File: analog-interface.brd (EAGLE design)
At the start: 160 x 100 mm, 18 parts, among them U1 ISL3179EIBZ, U2 ATMEGA328P

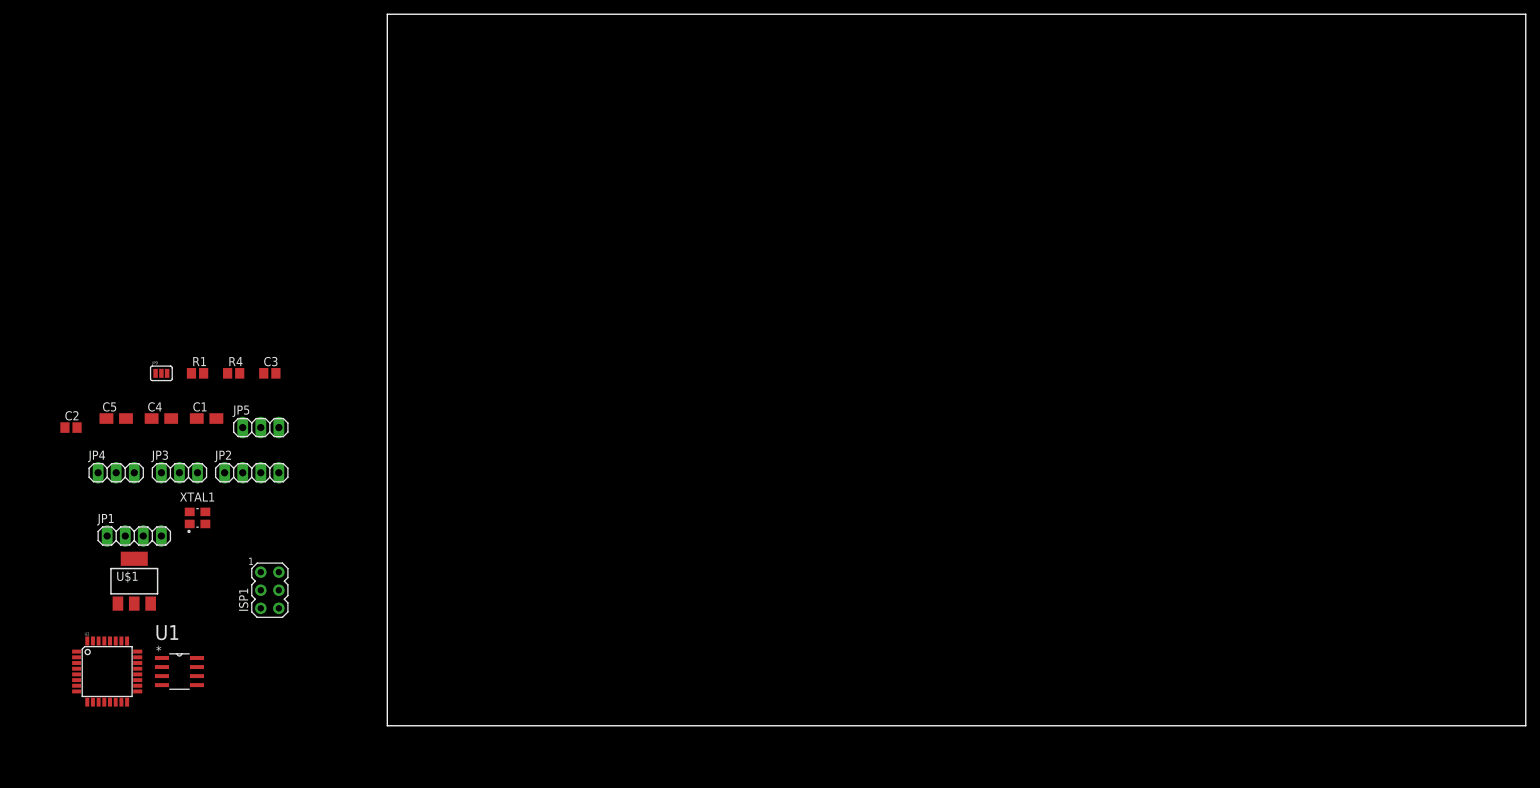
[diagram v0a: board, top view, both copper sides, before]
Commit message: done a lot of routing added vref chip
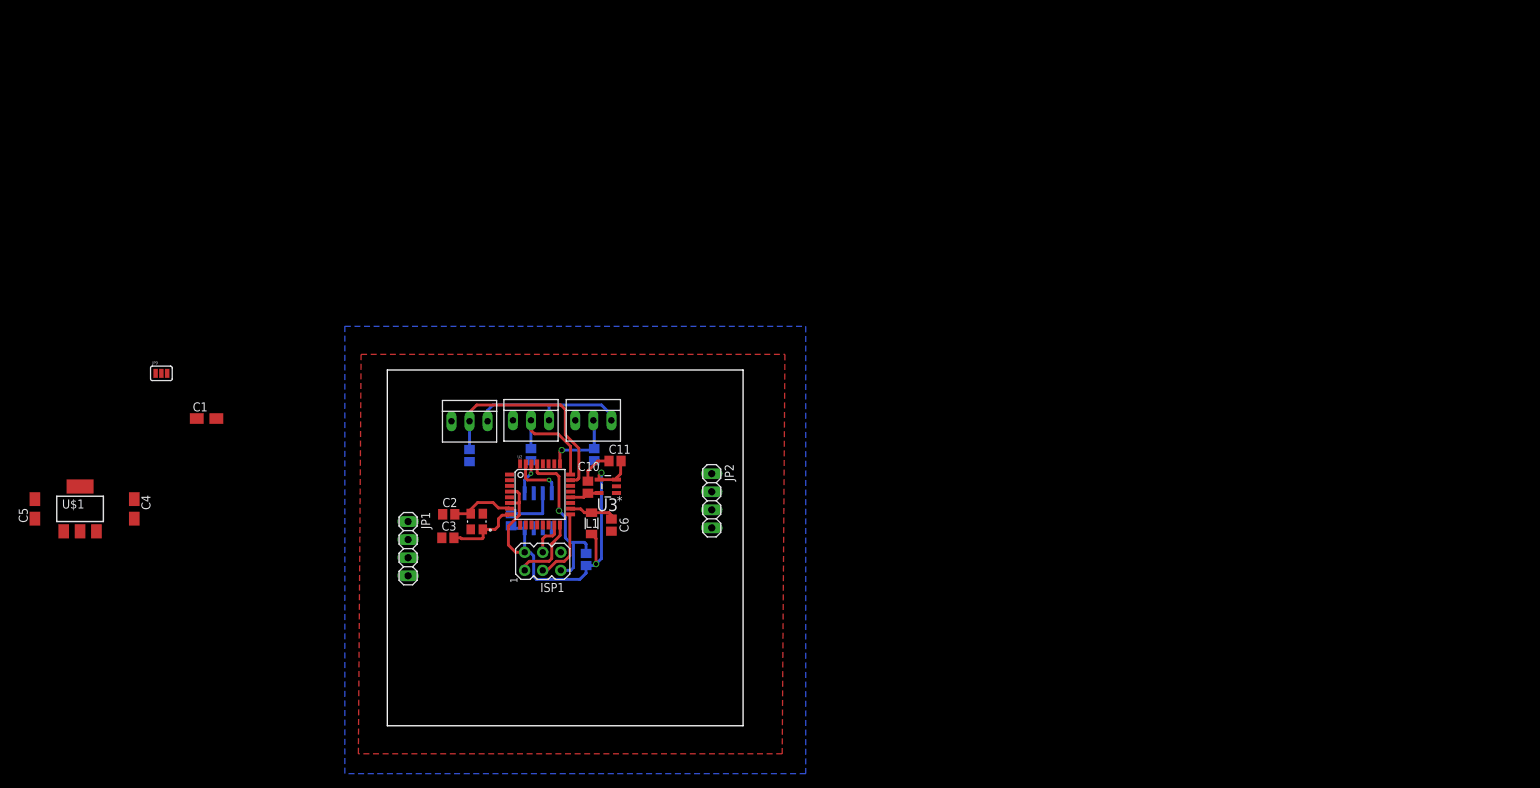
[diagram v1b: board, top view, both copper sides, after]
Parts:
- added C10: 22nF, resistor:C0805
- added C11: 100nF, resistor:C0805
- added C6, C7, C8, C9: 100uF, resistor:C0805
- added L1: 10uH, resistor:L3216C
- added U3: LM4120, mountainsensing:SOT23-5
- JP3: value (none) -> ADC0; device pinhead:1X03 -> farnell-parts:3-MOLEX
- JP4: value (none) -> ADC1; device pinhead:1X03 -> farnell-parts:3-MOLEX
- JP5: value (none) -> ADC2; device pinhead:1X03 -> farnell-parts:3-MOLEX
- moved U2 65.7 mm to (21.5, 32.5)
- moved JP2 64.8 mm to (45.6, 31.6), turned to 270 degrees
- moved JP4 58.8 mm to (20.2, 42.9), turned to 180 degrees
- moved R4 56.0 mm to (27.9, 23.4), flipped to the bottom, turned to 270 degrees
- moved U1 55.3 mm to (21.2, 30.2), flipped to the bottom, turned to 270 degrees
- moved C2 54.5 mm to (8.64, 29.7)
- moved R1 48.6 mm to (17.4, 29.0), flipped to the bottom, turned to 270 degrees
- moved JP5 46.7 mm to (29.0, 42.9), turned to 180 degrees
- moved JP3 41.4 mm to (11.6, 42.8), turned to 180 degrees
- moved XTAL1 39.2 mm to (12.6, 28.7), turned to 90 degrees
- moved ISP1 38.6 mm to (21.8, 23.1), turned to 90 degrees
- moved JP1 38.5 mm to (2.92, 24.9), turned to 270 degrees
- moved C3 34.1 mm to (8.51, 26.4)
- moved C5 17.1 mm to (-49.5, 30.5), turned to 90 degrees
- moved C4 13.3 mm to (-35.6, 30.5), turned to 270 degrees
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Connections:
- net AY renamed 485_P
- net BZ renamed 485_N
- new net N$4: C6.2, L1.1, U2.18
- new net N$7: C10.1, C11.1
- net ADC0: now also C7.2
- net ADC1: now also C8.2
- net ADC2: now also C9.2
- net AREF: now also C10.2, U3.5
- net GND: now also C6.1, C7.1, C8.1, C9.1, U3.2
- net VCC: now also C11.2, L1.2, U3.3, U3.4; no longer U2.18
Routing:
- net VCC: track 0.00 -> 81.5 mm, vias 0 -> 2
- net ADC0: track 0.00 -> 31.1 mm
- net !RESET: track 0.00 -> 23.6 mm, vias 0 -> 1
- net ADC1: track 0.00 -> 15.8 mm
- net ADC2: track 0.00 -> 10.7 mm, vias 0 -> 1
- net N$3: track 0.00 -> 10.6 mm
- net SCK: track 0.00 -> 10.5 mm
- net MISO: track 0.00 -> 10.1 mm
- net N$2: track 0.00 -> 9.07 mm
- net TX: track 0.00 -> 7.44 mm, vias 0 -> 1
- net N$1: track 0.00 -> 7.33 mm
- net N$4: track 0.00 -> 6.67 mm
- net MOSI: track 0.00 -> 5.13 mm
- net N$7: track 0.00 -> 4.97 mm
- net RX: track 0.00 -> 4.51 mm, vias 0 -> 1
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- added copper zone on layer 1, net GND
- added copper zone on layer 16, net GND
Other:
- board size 160 x 100 mm -> 50 x 50 mm
